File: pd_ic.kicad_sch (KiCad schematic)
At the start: 15 parts, among them J11 Conn_01x02, Q1 SiS443DN, U13 CYPD3175-24LQXQ, U17 TVS0500DRV

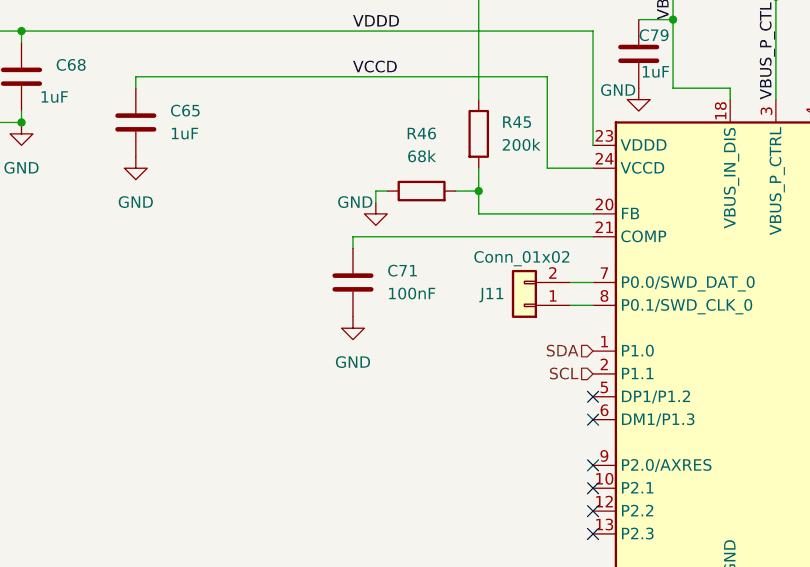
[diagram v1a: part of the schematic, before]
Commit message: added labels to everything
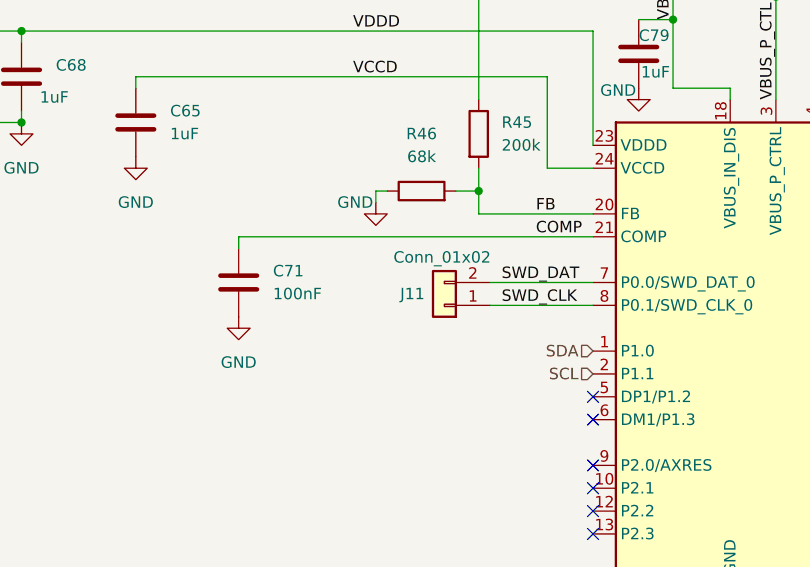
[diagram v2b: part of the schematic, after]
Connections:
- net SWD_CLK: now reaches J11.1 (Pin_1), U13.8 (P0.1/SWD_CLK_0)
- net SWD_DAT: now reaches J11.2 (Pin_2), U13.7 (P0.0/SWD_DAT_0)
- net COMP: now reaches C71.1, U13.21 (COMP)
- net FB: now reaches R45.2, R46.2, U13.20 (FB)
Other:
- moved on the sheet: C71, J11
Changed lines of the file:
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@@
 	(wire
 		(pts
-			(xy 135.89 99.06) (xy 138.43 99.06)
+			(xy 127 99.06) (xy 138.43 99.06)
 		)
 		(stroke
@@
 	(wire
 		(pts
-			(xy 138.43 91.44) (xy 111.76 91.44)
+			(xy 138.43 91.44) (xy 99.06 91.44)
 		)
 		(stroke
@@
 	(wire
 		(pts
-			(xy 111.76 91.44) (xy 111.76 92.71)
+			(xy 99.06 91.44) (xy 99.06 92.71)
 		)
 		(stroke
@@
 	(wire
 		(pts
-			(xy 135.89 96.52) (xy 138.43 96.52)
+			(xy 127 96.52) (xy 138.43 96.52)
 		)
 		(stroke
@@
 	(label "VBUS_P_CTL"
 		(at 158.75 76.2 90)
+		(effects
+			(font
+				(size 1.27 1.27)
+			)
+			(justify left bottom)
+		)
+	)
+	(label "SWD_DAT"
+		(at 128.27 96.52 0)
+		(effects
+			(font
+				(size 1.27 1.27)
+			)
+			(justify left bottom)
+		)
+	)
+	(label "SWD_CLK"
+		(at 128.27 99.06 0)
+		(effects
+			(font
+				(size 1.27 1.27)
+			)
+			(justify left bottom)
+		)
+	)
+	(label "COMP"
+		(at 132.08 91.44 0)
+		(effects
+			(font
+				(size 1.27 1.27)
+			)
+			(justify left bottom)
+		)
+	)
+	(label "FB"
+		(at 132.08 88.9 0)
 		(effects
 			(font
@@
 	(symbol
 		(lib_id "Connector_Generic:Conn_01x02")
-		(at 130.81 99.06 180)
+		(at 121.92 99.06 180)
 		(unit 1)
 		(exclude_from_sim no)
@@
 		(dnp no)
 		(property "Reference" "J11"
-			(at 127.254 97.79 0)
+			(at 118.364 97.79 0)
 			(effects
 				(font
@@
 		)
 		(property "Value" "Conn_01x02"
-			(at 130.556 93.726 0)
+			(at 121.666 93.726 0)
 			(effects
 				(font
@@
 		)
 		(property "Footprint" "Connector_PinHeader_2.54mm:PinHeader_1x02_P2.54mm_Vertical"
-			(at 130.81 99.06 0)
+			(at 121.92 99.06 0)
 			(effects
 				(font
@@
 		)
 		(property "Datasheet" "~"
-			(at 130.81 99.06 0)
+			(at 121.92 99.06 0)
 			(effects
 				(font
@@
 		)
 		(property "Description" "Generic connector, single row, 01x02, script generated (kicad-library-utils/schlib/autogen/connector/)"
-			(at 130.81 99.06 0)
+			(at 121.92 99.06 0)
 			(effects
 				(font
@@
 	(symbol
 		(lib_id "Device:C")
-		(at 111.76 96.52 0)
+		(at 99.06 96.52 0)
 		(unit 1)
 		(exclude_from_sim no)
@@
 		(fields_autoplaced yes)
 		(property "Reference" "C71"
-			(at 115.57 95.2499 0)
+			(at 102.87 95.2499 0)
 			(effects
 				(font
@@
 		)
 		(property "Value" "100nF"
-			(at 115.57 97.7899 0)
+			(at 102.87 97.7899 0)
 			(effects
 				(font
@@
 		)
 		(property "Footprint" "Capacitor_SMD:C_0402_1005Metric"
-			(at 112.7252 100.33 0)
+			(at 100.0252 100.33 0)
 			(effects
 				(font
@@
 		)
 		(property "Datasheet" "~"
-			(at 111.76 96.52 0)
+			(at 99.06 96.52 0)
 			(effects
 				(font
@@
 		)
 		(property "Description" "Unpolarized capacitor"
-			(at 111.76 96.52 0)
+			(at 99.06 96.52 0)
 			(effects
 				(font
@@
 	(symbol
 		(lib_id "power:GND")
-		(at 111.76 100.33 0)
+		(at 99.06 100.33 0)
 		(unit 1)
 		(exclude_from_sim no)
@@
 		(fields_autoplaced yes)
 		(property "Reference" "#PWR042"
-			(at 111.76 106.68 0)
+			(at 99.06 106.68 0)
 			(effects
 				(font
@@
 		)
 		(property "Value" "GND"
-			(at 111.76 105.41 0)
+			(at 99.06 105.41 0)
 			(effects
 				(font
@@
 		)
 		(property "Footprint" ""
-			(at 111.76 100.33 0)
+			(at 99.06 100.33 0)
 			(effects
 				(font
@@
 		)
 		(property "Datasheet" ""
-			(at 111.76 100.33 0)
+			(at 99.06 100.33 0)
 			(effects
 				(font
@@
 		)
 		(property "Description" "Power symbol creates a global label with name \"GND\" , ground"
-			(at 111.76 100.33 0)
-			(effects
-				(font
+			(at 99.06 100.33 0)
+			(effects
+				(font

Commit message: changes
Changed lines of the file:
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@@
+	)
+	(junction
+		(at 147.32 66.04)
+		(diameter 0)
+		(color 0 0 0 0)
 	)
 	(junction
@@
 	)
 	(junction
-		(at 147.32 67.31)
-		(diameter 0)
-		(color 0 0 0 0)
-	)
-	(junction
 		(at 147.32 54.61)
 		(diameter 0)
@@
 	(wire
 		(pts
-			(xy 147.32 67.31) (xy 147.32 74.93)
-		)
-		(stroke
-			(width 0)
-			(type default)
-		)
-	)
-	(wire
-		(pts
 			(xy 127 99.06) (xy 138.43 99.06)
 		)
@@
 	(wire
 		(pts
+			(xy 147.32 66.04) (xy 147.32 74.93)
+		)
+		(stroke
+			(width 0)
+			(type default)
+		)
+	)
+	(wire
+		(pts
 			(xy 163.83 54.61) (xy 166.37 54.61)
 		)
@@
 	(wire
 		(pts
-			(xy 143.51 67.31) (xy 147.32 67.31)
+			(xy 143.51 66.04) (xy 147.32 66.04)
 		)
 		(stroke
@@
 	(wire
 		(pts
+			(xy 143.51 66.04) (xy 143.51 67.31)
+		)
+		(stroke
+			(width 0)
+			(type default)
+		)
+	)
+	(wire
+		(pts
 			(xy 158.75 64.77) (xy 158.75 76.2)
 		)
@@
 	(wire
 		(pts
-			(xy 147.32 54.61) (xy 147.32 67.31)
+			(xy 147.32 54.61) (xy 147.32 66.04)
 		)
 		(stroke
@@
 		(effects
 			(font
-				(size 1.27 1.27)
-			)
-			(justify left bottom)
-		)
-	)
-	(label "VBUS_IN_DIS"
-		(at 147.32 67.31 90)
-		(effects
-			(font

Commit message: added some lcsc part ids
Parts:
- Q1: LCSC (none) -> C142539
- U13: LCSC (none) -> C2952419
- U17: LCSC (none) -> C609571
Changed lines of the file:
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@@
+			)
+		)
+		(property "LCSC" "C609571"
+			(at 186.69 63.5 0)
+			(effects
+				(font
+					(size 1.27 1.27)
+				)
+				(hide yes)
 			)
 		)
@@
 			)
 		)
+		(property "LCSC" "C2952419"
+			(at 161.29 104.14 0)
+			(effects
+				(font
+					(size 1.27 1.27)
+				)
+				(hide yes)
+			)
+		)
 		(pin "21"
 		)
@@
 			(effects
 				(font
+					(size 1.27 1.27)
+				)
+				(hide yes)
+			)
+		)
+		(property "LCSC" "C142539"
+			(at 158.75 57.15 90)
+			(effects
+				(font

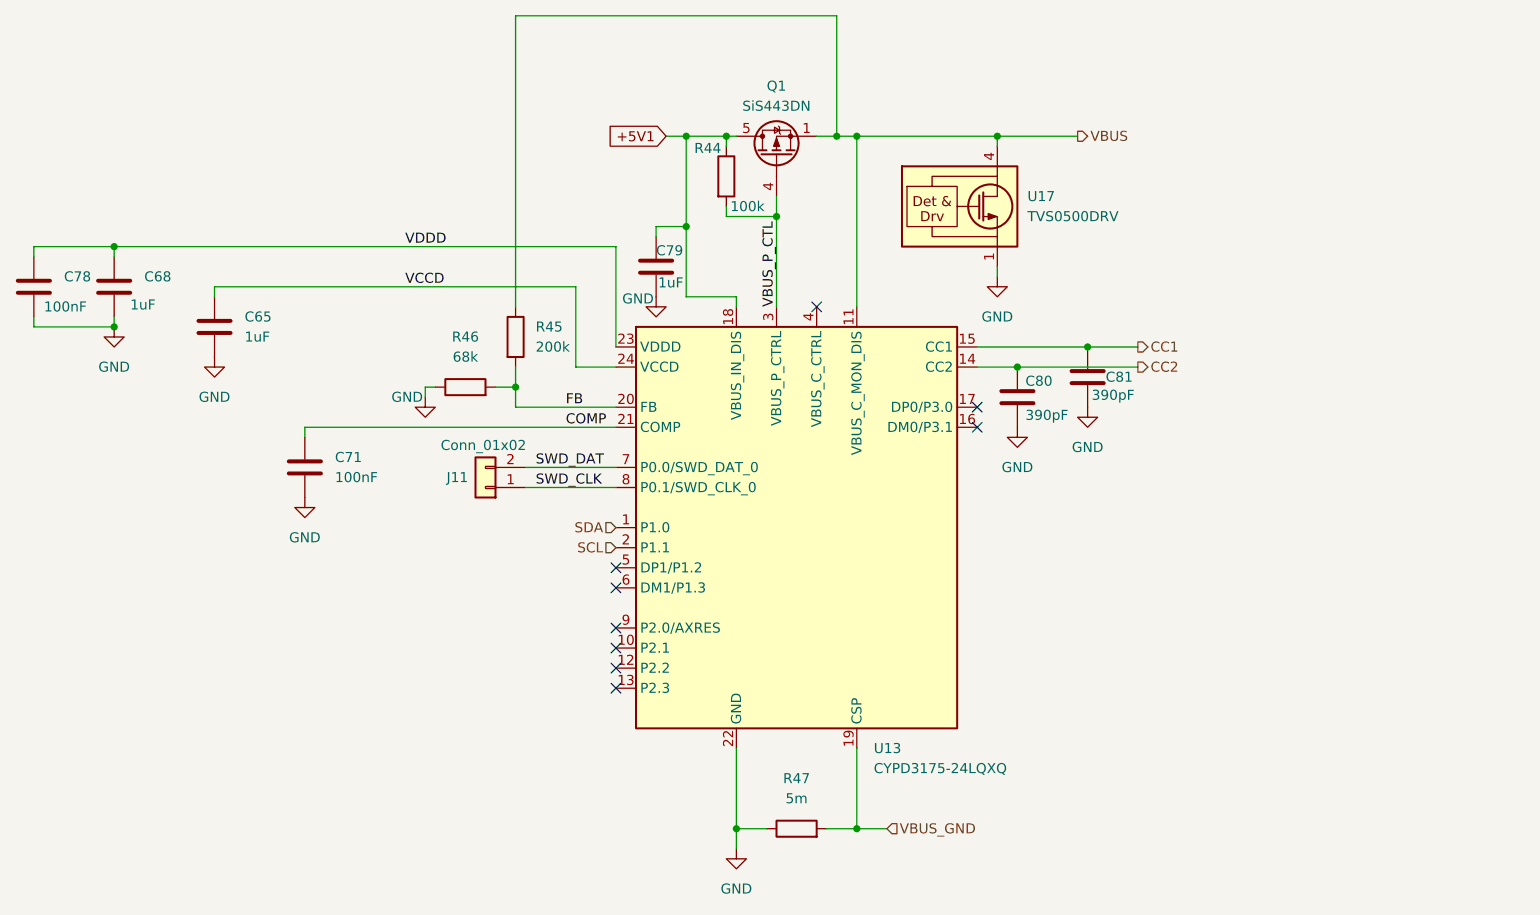
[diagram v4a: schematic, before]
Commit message: moved usb c port to edge
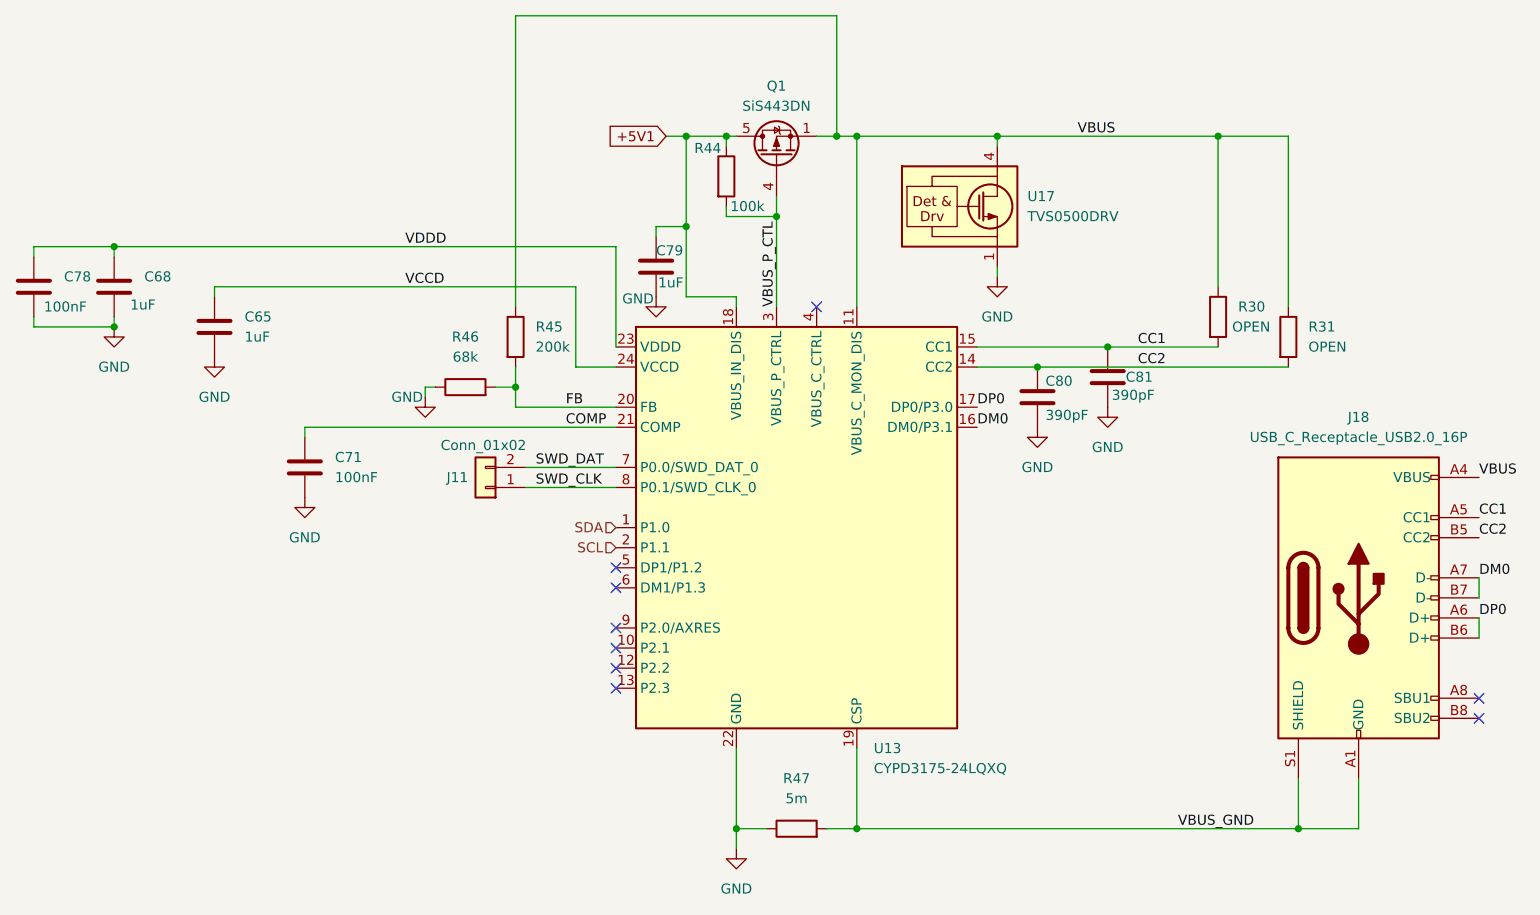
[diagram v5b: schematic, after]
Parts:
- added J18: USB_C_Receptacle_USB2.0_16P, Connector_USB:USB_C_Receptacle_GCT_USB4105-xx-A_16P_TopMnt_Horizontal, symbol Connector:USB_C_Receptacle_USB2.0_16P
- added R30, R31: OPEN, Resistor_SMD:R_0402_1005Metric, symbol Device:R
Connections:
- net CC1: now also J18.A5 (CC1), R30.2
- net CC2: now also J18.B5 (CC2), R31.2
- net VBUS: now also J18.A4 (VBUS), J18.A9 (VBUS), J18.B4 (VBUS), J18.B9 (VBUS), R30.1, R31.1
- net VBUS_GND: now also J18.A1 (GND), J18.A12 (GND), J18.B1 (GND), J18.B12 (GND), J18.S1 (SHIELD)
- net DM0: now reaches U13.16 (DM0/P3.1)
- net DM0: now also J18.A7 (D-), J18.B7 (D-)
- net DP0: now reaches U13.17 (DP0/P3.0)
- net DP0: now also J18.A6 (D+), J18.B6 (D+)
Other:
- moved on the sheet: C80, C81

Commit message: added open pull down resistor to allow disabling usb pd controller
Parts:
- added R7: OPEN, Resistor_SMD:R_0402_1005Metric, symbol Device:R
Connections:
- net GND: now also R7.2
- net VBUS_P_CTL: now also R7.1
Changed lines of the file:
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@@
+	)
+	(junction
+		(at 158.75 62.23)
+		(diameter 0)
+		(color 0 0 0 0)
 	)
 	(junction
@@
 		(pts
 			(xy 74.93 68.58) (xy 74.93 69.85)
+		)
+		(stroke
+			(width 0)
+			(type default)
+		)
+	)
+	(wire
+		(pts
+			(xy 158.75 62.23) (xy 162.56 62.23)
 		)
 		(stroke
@@
 	)
 	(symbol
+		(lib_id "power:GND")
+		(at 162.56 69.85 0)
+		(unit 1)
+		(exclude_from_sim no)
+		(in_bom yes)
+		(on_board yes)
+		(dnp no)
+		(property "Reference" "#PWR019"
+			(at 162.56 76.2 0)
+			(effects
+				(font
+					(size 1.27 1.27)
+				)
+				(hide yes)
+			)
+		)
+		(property "Value" "GND"
+			(at 164.592 70.104 0)
+			(effects
+				(font
+					(size 1.27 1.27)
+				)
+			)
+		)
+		(property "Footprint" ""
+			(at 162.56 69.85 0)
+			(effects
+				(font
+					(size 1.27 1.27)
+				)
+				(hide yes)
+			)
+		)
+		(property "Datasheet" ""
+			(at 162.56 69.85 0)
+			(effects
+				(font
+					(size 1.27 1.27)
+				)
+				(hide yes)
+			)
+		)
+		(property "Description" "Power symbol creates a global label with name \"GND\" , ground"
+			(at 162.56 69.85 0)
+			(effects
+				(font
+					(size 1.27 1.27)
+				)
+				(hide yes)
+			)
+		)
+		(pin "1"
+		)
+		(instances
+			(project ""
+				(path "/2f56b371-1597-47e1-a48d-b7f69d342f77/a0987cd4-dfa7-4cf4-a9f1-5b392786bba7"
+					(reference "#PWR019")
+					(unit 1)
+				)
+			)
+		)
+	)
+	(symbol
 		(lib_id "Device:C")
 		(at 99.06 96.52 0)
@@
 					(unit 1)
 				)
+			)
+		)
+	)
+	(symbol
+		(lib_id "Device:R")
+		(at 162.56 66.04 0)
+		(unit 1)
+		(exclude_from_sim no)
+		(in_bom yes)
+		(on_board yes)
+		(dnp no)
+		(property "Reference" "R7"
+			(at 163.576 64.77 0)
+			(effects
+				(font
+					(size 1.27 1.27)
+				)
+				(justify left)
+			)
+		)
+		(property "Value" "OPEN"
+			(at 163.576 67.31 0)
+			(effects
+				(font
+					(size 1.27 1.27)
+				)
+				(justify left)
+			)
+		)
+		(property "Footprint" "Resistor_SMD:R_0402_1005Metric"
+			(at 160.782 66.04 90)
+			(effects
+				(font
+					(size 1.27 1.27)
+				)
+				(hide yes)
+			)
+		)
+		(property "Datasheet" "~"
+			(at 162.56 66.04 0)
+			(effects
+				(font
+					(size 1.27 1.27)
+				)
+				(hide yes)
+			)
+		)
+		(property "Description" "Resistor"
+			(at 162.56 66.04 0)
+			(effects
+				(font
+					(size 1.27 1.27)
+				)
+				(hide yes)
+			)
+		)
+		(pin "1"
+		)
+		(pin "2"
+		)
+		(instances
+			(project ""
+				(path "/2f56b371-1597-47e1-a48d-b7f69d342f77/a0987cd4-dfa7-4cf4-a9f1-5b392786bba7"
+					(reference "R7")
+					(unit 1)
+				)

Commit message: fixed some issues with crystals and other stuff
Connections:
- net +5V1: now also Q1.1 (S), Q1.2 (S), Q1.3 (S); no longer Q1.5 (D)
- net VBUS: now also Q1.5 (D); no longer Q1.1 (S), Q1.2 (S), Q1.3 (S)
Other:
- moved on the sheet: Q1
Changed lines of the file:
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@@
 	(symbol
 		(lib_id "Transistor_FET:SiS443DN")
-		(at 158.75 57.15 90)
+		(at 158.75 57.15 270)
+		(mirror x)
 		(unit 1)
 		(exclude_from_sim no)
@@
 		(on_board yes)
 		(dnp no)
-		(fields_autoplaced yes)
 		(property "Reference" "Q1"
 			(at 158.75 48.26 90)
@@
 		)
 		(property "Footprint" "Package_SO:Vishay_PowerPAK_1212-8_Single"
-			(at 160.655 52.07 0)
+			(at 156.845 52.07 0)
 			(effects
 				(font
@@
 		)
 		(property "Datasheet" "https://www.vishay.com/docs/63253/sis443dn.pdf"
-			(at 162.56 52.07 0)
+			(at 154.94 52.07 0)
 			(effects
 				(font

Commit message: more lcsc
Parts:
- C71, C78: LCSC (none) -> C1525
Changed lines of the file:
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@@
+			)
+		)
+		(property "LCSC" "C1525"
+			(at 99.06 96.52 0)
+			(effects
+				(font
+					(size 1.27 1.27)
+				)
+				(hide yes)
 			)
 		)
@@
 			(at 64.77 73.66 0)
 			(effects
+				(font
+					(size 1.27 1.27)
+				)
+				(hide yes)
+			)
+		)
+		(property "LCSC" "C1525"
+			(at 64.77 73.66 0)
+			(effects
